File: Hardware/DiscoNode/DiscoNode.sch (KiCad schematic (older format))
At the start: 68 parts, among them IC1 ATMEGA328P, J1 1267, J2 RJ45, J3 RJ45, J4 AVR-ISP-6, J5 Debug, J6 0026605020, Q1 NTR4003N, Q2 NTR4003N, Q3 NTR4003N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

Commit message: Fix LEDs
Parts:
- D1, D10, D11, D12, D13, D14, D15, D16, D17, D18, D2, D3, D4, D5, D6, D7, D8, D9: footprint LEDs:LED_RGB_PLCC-6 -> LEDs:LED_WS2812-PLCC6
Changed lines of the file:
@@
 F 0 "D1" H 1950 8770 50  0000 C CNN
 F 1 "SLV6A-FKB" H 1950 8050 50  0000 C CNN
-F 2 "LEDs:LED_RGB_PLCC-6" H 1950 8350 50  0001 C CNN
+F 2 "LEDs:LED_WS2812-PLCC6" H 1950 8350 50  0001 C CNN
 F 3 "" H 1950 8350 50  0000 C CNN
 	1    1950 8400
@@
 F 0 "D2" H 1950 9220 50  0000 C CNN
 F 1 "SLV6A-FKB" H 1950 8500 50  0001 C CNN
-F 2 "LEDs:LED_RGB_PLCC-6" H 1950 8800 50  0001 C CNN
+F 2 "LEDs:LED_WS2812-PLCC6" H 1950 8800 50  0001 C CNN
 F 3 "" H 1950 8800 50  0000 C CNN
 	1    1950 8850
@@
 F 0 "D3" H 1950 9670 50  0000 C CNN
 F 1 "SLV6A-FKB" H 1950 8950 50  0001 C CNN
-F 2 "LEDs:LED_RGB_PLCC-6" H 1950 9250 50  0001 C CNN
+F 2 "LEDs:LED_WS2812-PLCC6" H 1950 9250 50  0001 C CNN
 F 3 "" H 1950 9250 50  0000 C CNN
 	1    1950 9300
@@
 F 0 "D4" H 2800 8770 50  0000 C CNN
 F 1 "SLV6A-FKB" H 2800 8050 50  0001 C CNN
-F 2 "LEDs:LED_RGB_PLCC-6" H 2800 8350 50  0001 C CNN
+F 2 "LEDs:LED_WS2812-PLCC6" H 2800 8350 50  0001 C CNN
 F 3 "" H 2800 8350 50  0000 C CNN
 	1    2800 8400
@@
 F 0 "D5" H 2800 9220 50  0000 C CNN
 F 1 "SLV6A-FKB" H 2800 8500 50  0001 C CNN
-F 2 "LEDs:LED_RGB_PLCC-6" H 2800 8800 50  0001 C CNN
+F 2 "LEDs:LED_WS2812-PLCC6" H 2800 8800 50  0001 C CNN
 F 3 "" H 2800 8800 50  0000 C CNN
 	1    2800 8850
@@
 F 0 "D6" H 2800 9670 50  0000 C CNN
 F 1 "SLV6A-FKB" H 2800 8950 50  0001 C CNN
-F 2 "LEDs:LED_RGB_PLCC-6" H 2800 9250 50  0001 C CNN
+F 2 "LEDs:LED_WS2812-PLCC6" H 2800 9250 50  0001 C CNN
 F 3 "" H 2800 9250 50  0000 C CNN
 	1    2800 9300
@@
 F 0 "D7" H 3650 8770 50  0000 C CNN
 F 1 "SLV6A-FKB" H 3650 8050 50  0001 C CNN
-F 2 "LEDs:LED_RGB_PLCC-6" H 3650 8350 50  0001 C CNN
+F 2 "LEDs:LED_WS2812-PLCC6" H 3650 8350 50  0001 C CNN
 F 3 "" H 3650 8350 50  0000 C CNN
 	1    3650 8400
@@
 F 0 "D8" H 3650 9220 50  0000 C CNN
 F 1 "SLV6A-FKB" H 3650 8500 50  0001 C CNN
-F 2 "LEDs:LED_RGB_PLCC-6" H 3650 8800 50  0001 C CNN
+F 2 "LEDs:LED_WS2812-PLCC6" H 3650 8800 50  0001 C CNN
 F 3 "" H 3650 8800 50  0000 C CNN
 	1    3650 8850
@@
 F 0 "D9" H 3650 9670 50  0000 C CNN
 F 1 "SLV6A-FKB" H 3650 8950 50  0001 C CNN
-F 2 "LEDs:LED_RGB_PLCC-6" H 3650 9250 50  0001 C CNN
+F 2 "LEDs:LED_WS2812-PLCC6" H 3650 9250 50  0001 C CNN
 F 3 "" H 3650 9250 50  0000 C CNN
 	1    3650 9300
@@
 F 0 "D10" H 4500 8770 50  0000 C CNN
 F 1 "SLV6A-FKB" H 4500 8050 50  0001 C CNN
-F 2 "LEDs:LED_RGB_PLCC-6" H 4500 8350 50  0001 C CNN
+F 2 "LEDs:LED_WS2812-PLCC6" H 4500 8350 50  0001 C CNN
 F 3 "" H 4500 8350 50  0000 C CNN
 	1    4500 8400
@@
 F 0 "D11" H 4500 9220 50  0000 C CNN
 F 1 "SLV6A-FKB" H 4500 8500 50  0001 C CNN
-F 2 "LEDs:LED_RGB_PLCC-6" H 4500 8800 50  0001 C CNN
+F 2 "LEDs:LED_WS2812-PLCC6" H 4500 8800 50  0001 C CNN
 F 3 "" H 4500 8800 50  0000 C CNN
 	1    4500 8850
@@
 F 0 "D12" H 4500 9670 50  0000 C CNN
 F 1 "SLV6A-FKB" H 4500 8950 50  0001 C CNN
-F 2 "LEDs:LED_RGB_PLCC-6" H 4500 9250 50  0001 C CNN
+F 2 "LEDs:LED_WS2812-PLCC6" H 4500 9250 50  0001 C CNN
 F 3 "" H 4500 9250 50  0000 C CNN
 	1    4500 9300
@@
 F 0 "D13" H 5300 8770 50  0000 C CNN
 F 1 "SLV6A-FKB" H 5300 8050 50  0001 C CNN
-F 2 "LEDs:LED_RGB_PLCC-6" H 5300 8350 50  0001 C CNN
+F 2 "LEDs:LED_WS2812-PLCC6" H 5300 8350 50  0001 C CNN
 F 3 "" H 5300 8350 50  0000 C CNN
 	1    5300 8400
@@
 F 0 "D14" H 5300 9220 50  0000 C CNN
 F 1 "SLV6A-FKB" H 5300 8500 50  0001 C CNN
-F 2 "LEDs:LED_RGB_PLCC-6" H 5300 8800 50  0001 C CNN
+F 2 "LEDs:LED_WS2812-PLCC6" H 5300 8800 50  0001 C CNN
 F 3 "" H 5300 8800 50  0000 C CNN
 	1    5300 8850
@@
 F 0 "D15" H 5300 9670 50  0000 C CNN
 F 1 "SLV6A-FKB" H 5300 8950 50  0001 C CNN
-F 2 "LEDs:LED_RGB_PLCC-6" H 5300 9250 50  0001 C CNN
+F 2 "LEDs:LED_WS2812-PLCC6" H 5300 9250 50  0001 C CNN
 F 3 "" H 5300 9250 50  0000 C CNN
 	1    5300 9300
@@
 F 0 "D16" H 6150 8770 50  0000 C CNN
 F 1 "SLV6A-FKB" H 6150 8050 50  0001 C CNN
-F 2 "LEDs:LED_RGB_PLCC-6" H 6150 8350 50  0001 C CNN
+F 2 "LEDs:LED_WS2812-PLCC6" H 6150 8350 50  0001 C CNN
 F 3 "" H 6150 8350 50  0000 C CNN
 	1    6150 8400
@@
 F 0 "D17" H 6150 9220 50  0000 C CNN
 F 1 "SLV6A-FKB" H 6150 8500 50  0001 C CNN
-F 2 "LEDs:LED_RGB_PLCC-6" H 6150 8800 50  0001 C CNN
+F 2 "LEDs:LED_WS2812-PLCC6" H 6150 8800 50  0001 C CNN
 F 3 "" H 6150 8800 50  0000 C CNN
 	1    6150 8850
@@
 F 0 "D18" H 6150 9670 50  0000 C CNN
 F 1 "SLV6A-FKB" H 6150 8950 50  0001 C CNN
-F 2 "LEDs:LED_RGB_PLCC-6" H 6150 9250 50  0001 C CNN
+F 2 "LEDs:LED_WS2812-PLCC6" H 6150 9250 50  0001 C CNN
 F 3 "" H 6150 9250 50  0000 C CNN
 	1    6150 9300

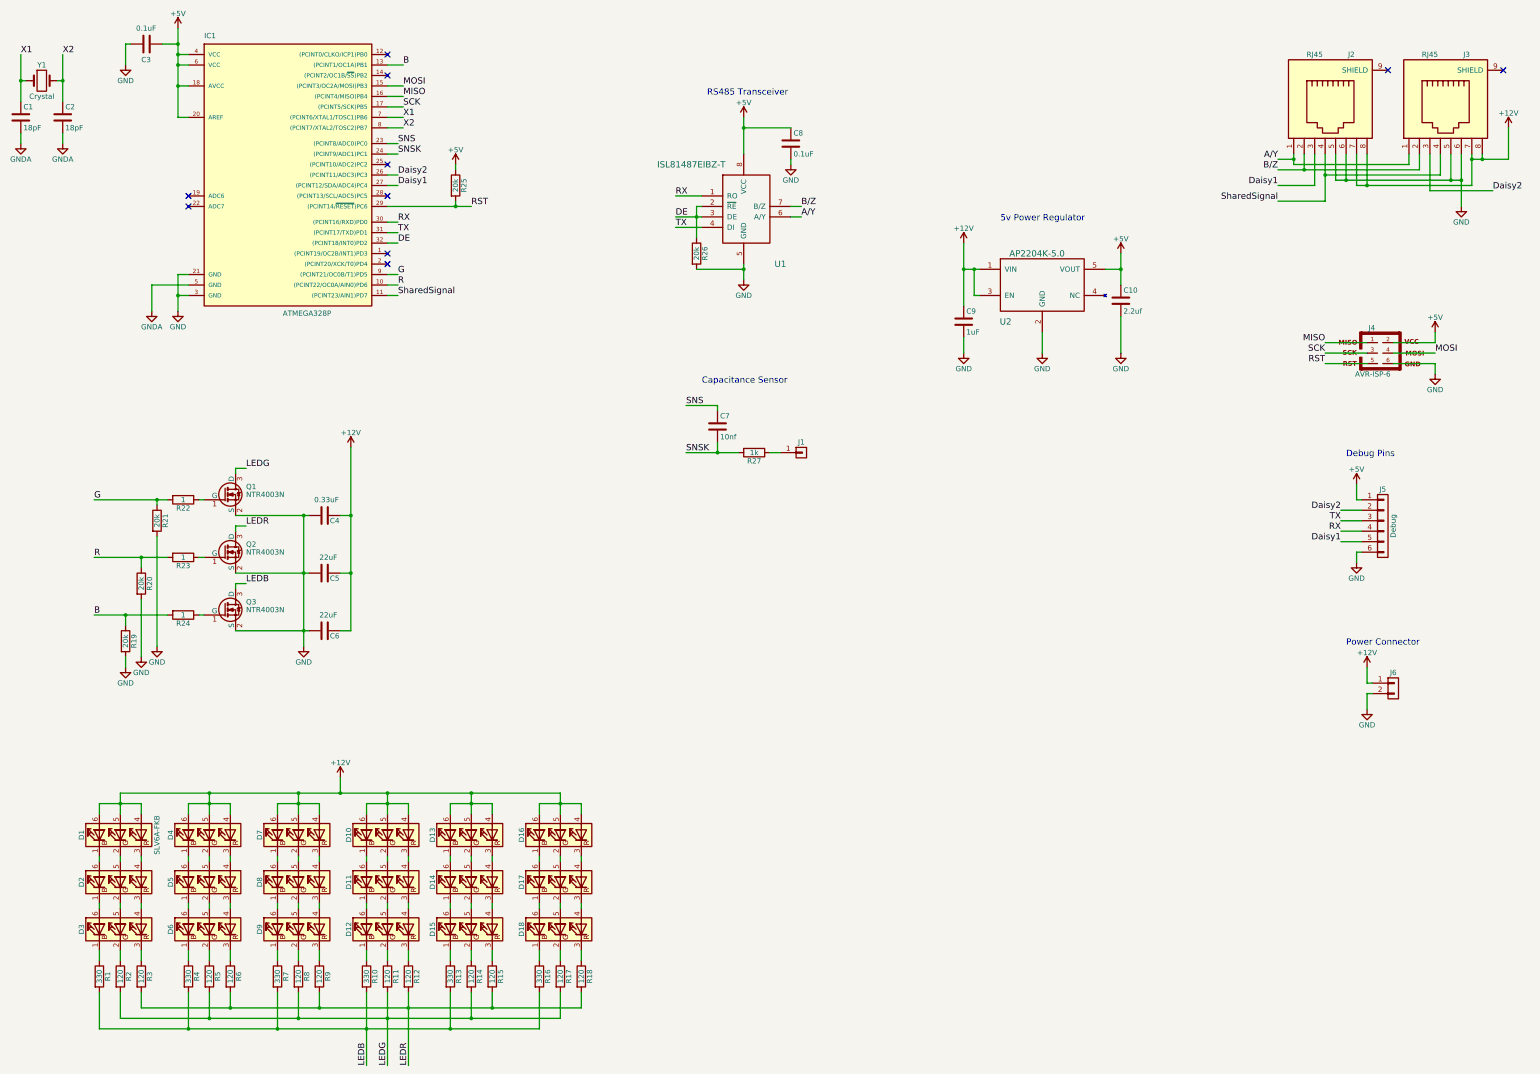
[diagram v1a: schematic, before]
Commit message: Update LED & Crystal footprints. Change LED resistor placement.
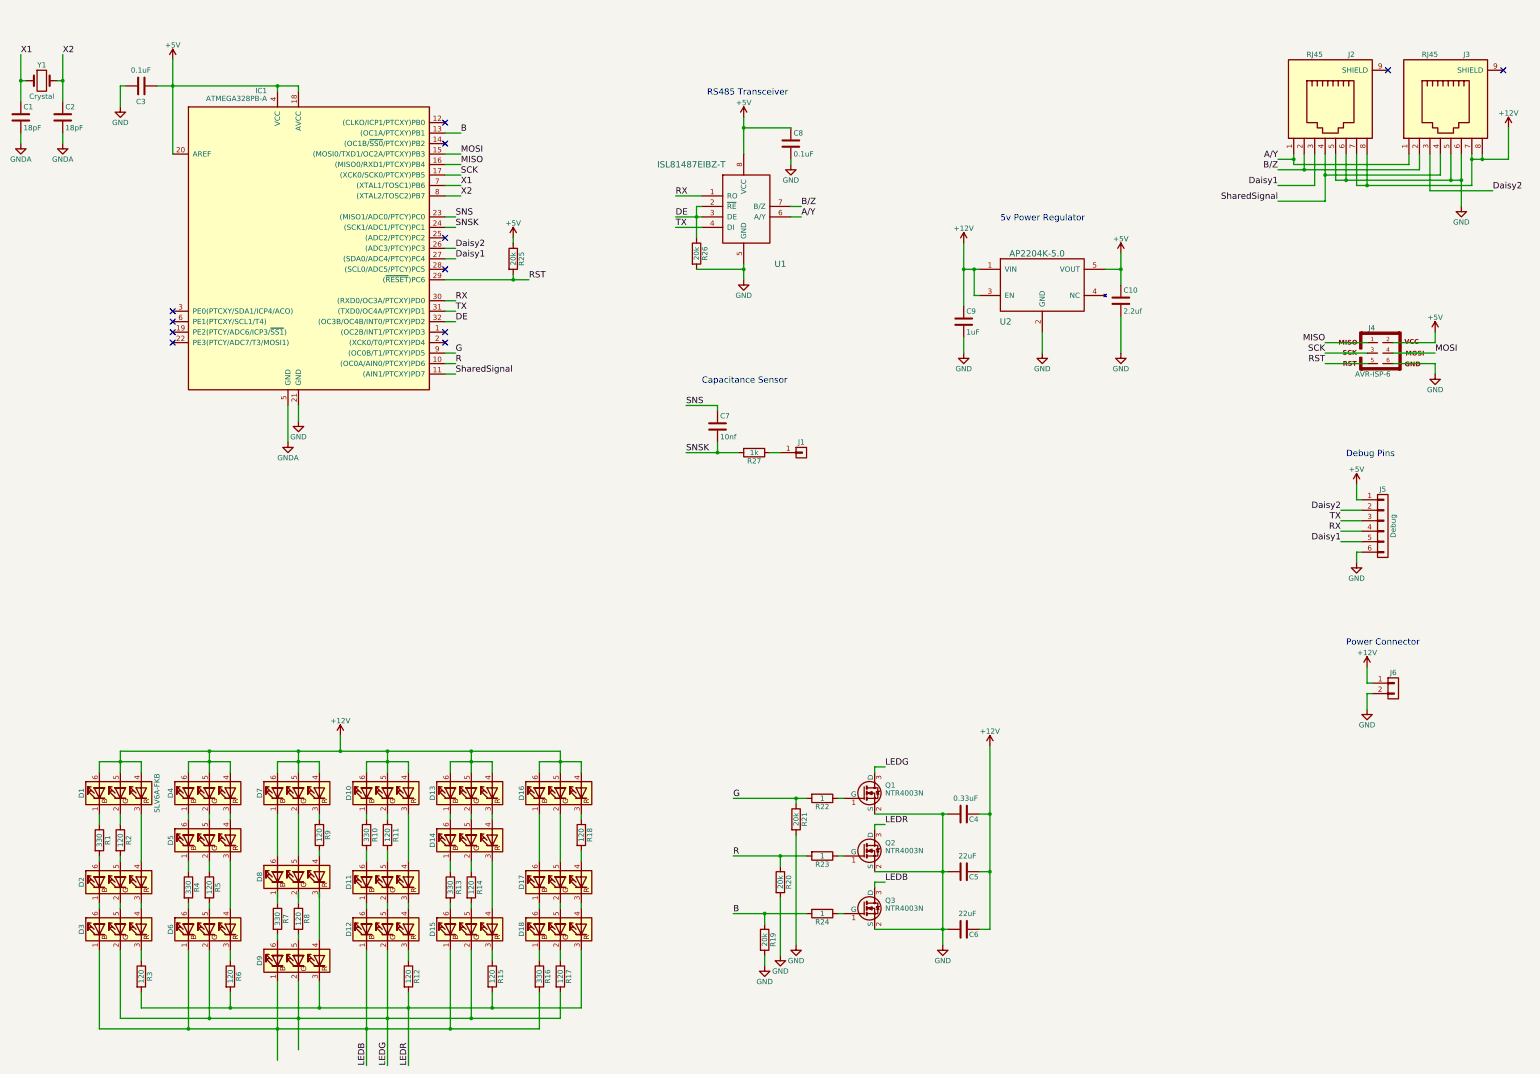
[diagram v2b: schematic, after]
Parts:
- removed IC1: ATMEGA328P, Housings_QFP:TQFP-32_7x7mm_Pitch0.8mm, symbol ATMEGA328P-A
- added IC1: ATMEGA328PB-A, Housings_QFP:TQFP-32_7x7mm_Pitch0.8mm, symbol ATMEGA328PB-A
- D1, D10, D11, D12, D13, D14, D15, D16, D17, D18, D2, D3, D4, D5, D6, D7, D8, D9: footprint LEDs:LED_WS2812-PLCC6 -> DiscoNode:LED_RGB-PLCC6-5.5x5.3mm
- R27: footprint Resistors_SMD:R_0805 -> Resistors_SMD:R_0805_HandSoldering
- Y1: footprint Crystals:Crystal_SMD_7050-2pin_7.0x5.0mm -> DiscoNode:Crystal_SMD_2pin_7.0x4.1mm
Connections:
- net +5V: now also IC1.18 (AVCC), IC1.20 (AREF), IC1.4 (VCC)
- net B: now also IC1.13 ((OC1A/PTCXY)PB1)
- net DE: now also IC1.32 ((OC3B/OC4B/INT0/PTCXY)PD2)
- net Daisy1: now also IC1.27 ((SDA0/ADC4/PTCY)PC4)
- net Daisy2: now also IC1.26 ((ADC3/PTCY)PC3)
- net G: now also IC1.9 ((OC0B/T1/PTCXY)PD5)
- net GND: now also IC1.21 (GND)
- net GNDA: now also IC1.5 (GND)
- net LEDB: now also D12.1 (RK), D15.1 (RK), D3.1 (RK), D6.1 (RK), D9.1 (RK); no longer R1.2, R10.2, R13.2, R4.2, R7.2
- net LEDG: now also D12.2 (GK), D15.2 (GK), D3.2 (GK), D6.2 (GK), D9.2 (GK); no longer R11.2, R14.2, R2.2, R5.2, R8.2
- net LEDR: now also D18.3 (BK), D9.3 (BK); no longer R18.2, R9.2
- net MISO: now also IC1.16 ((MISO0/RXD1/PTCXY)PB4)
- net MOSI: now also IC1.15 ((MOSI0/TXD1/OC2A/PTCXY)PB3)
- net R: now also IC1.10 ((OC0A/AIN0/PTCXY)PD6)
- net RST: now also IC1.29 ((~RESET~)PC6)
- net RX: now also IC1.30 ((RXD0/OC3A/PTCXY)PD0)
- net SCK: now also IC1.17 ((XCK0/SCK0/PTCXY)PB5)
- net SNS: now also IC1.23 ((MISO1/ADC0/PTCY)PC0)
- net SNSK: now also IC1.24 ((SCK1/ADC1/PTCY)PC1)
- net SharedSignal: now also IC1.11 ((AIN1/PTCXY)PD7)
- net TX: now also IC1.31 ((TXD0/OC4A/PTCXY)PD1)
- net X1: now also IC1.7 ((XTAL1/TOSC1)PB6)
- net X2: now also IC1.8 ((XTAL2/TOSC2)PB7)
- net at D1.1 (RK): now also R1.1; no longer D2.6 (RA)
- net at D1.2 (GK): now also R2.1; no longer D2.5 (GA)
- net at D5.1 (RK): now also R4.1; no longer D6.6 (RA)
- net at D5.2 (GK): now also R5.1; no longer D6.5 (GA)
- net at D7.3 (BK): now also R9.2; no longer D8.4 (BA)
- net at D8.1 (RK): no longer D9.6 (RA)
- net at D8.2 (GK): no longer D9.5 (GA)
- net at D8.3 (BK): no longer D9.4 (BA)
- net at R7.1: no longer D9.1 (RK)
- net at R8.1: no longer D9.2 (GK)
- net at R9.1: now also D8.4 (BA); no longer D9.3 (BK)
- net at D10.1 (RK): now also R10.1; no longer D11.6 (RA)
- net at D10.2 (GK): now also R11.1; no longer D11.5 (GA)
- net at D14.1 (RK): now also R13.1; no longer D15.6 (RA)
- net at D14.2 (GK): now also R14.1; no longer D15.5 (GA)
- net at D16.3 (BK): now also R18.1; no longer D17.4 (BA)
- new net: D2.5 (GA), R2.2
- new net: D2.6 (RA), R1.2
- new net: D6.5 (GA), R5.2
- new net: D6.6 (RA), R4.2
- new net: D9.5 (GA), R8.2
- new net: D9.6 (RA), R7.2
- new net: D11.5 (GA), R11.2
- new net: D11.6 (RA), R10.2
- new net: D15.5 (GA), R14.2
- new net: D15.6 (RA), R13.2
- new net: D17.4 (BA), R18.2
- no-connect marks 10 -> 12
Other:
- moved on the sheet: C3, C4, C5, C6, D1, D10, D13, D14, D16, D4, D5, D7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

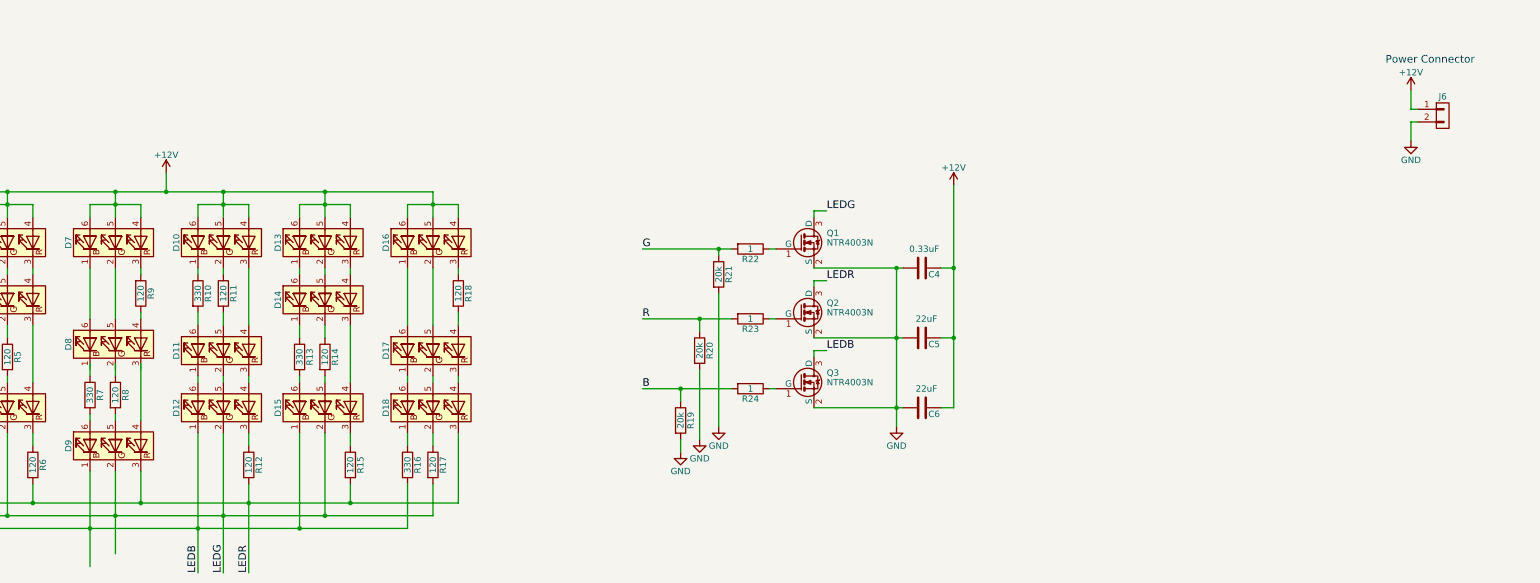
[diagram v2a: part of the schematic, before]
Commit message: Move RJ45 jacks to edge of board.
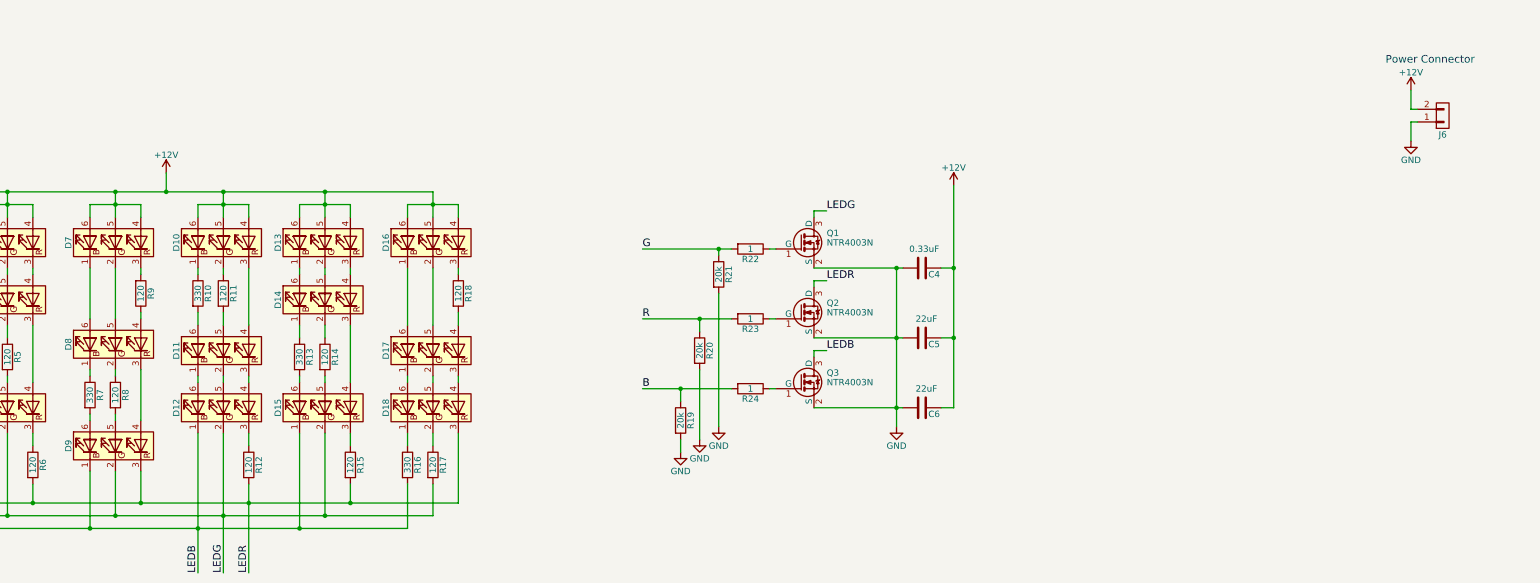
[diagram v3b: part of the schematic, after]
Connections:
- net +12V: now also J6.2 (P2); no longer J6.1 (P1)
- net GND: now also J6.1 (P1); no longer J6.2 (P2)
- net at D8.1 (RK): now also R7.1
- net at D8.2 (GK): now also R8.1
- net at D8.3 (BK): now also D9.4 (BA)
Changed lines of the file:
@@
 F 6 "WM4640-ND" H 14100 7000 60  0001 C CNN "Digikey"
 	1    14100 7000
-	1    0    0    -1
+	1    0    0    1
 $EndComp
 $Comp
@@
 	4300 9500 4300 10600
 Connection ~ 4300 10250
-Wire Wire Line
-	3650 9800 3650 10450
 Connection ~ 3650 10150
-Wire Wire Line
-	3450 9800 3450 10550
 Connection ~ 3450 10250
 Wire Wire Line
@@
 Wire Wire Line
 	2150 9050 2150 9100
-Wire Wire Line
-	3450 8950 3450 9050
-Wire Wire Line
-	3650 9050 3650 8950
-Wire Wire Line
-	3850 8950 3850 9400
 Wire Wire Line
 	3650 4300 3650 4450
@@
 Wire Wire Line
 	3850 8550 3850 8600
+Wire Wire Line
+	3450 9000 3450 9050
+Wire Wire Line
+	3650 9000 3650 9050
+Wire Wire Line
+	3850 9000 3850 9400
+Wire Wire Line
+	3650 9800 3650 10150
+Wire Wire Line
+	3450 9800 3450 10250
 $EndSCHEMATC
